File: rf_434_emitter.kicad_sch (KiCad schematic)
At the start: 67 parts, among them J1 Conn_Coaxial, J2 Jack-DC, SW1 SW_DIP_x06, SW5 SW_SPDT, SW7 SW_SPDT, SW8 SW_SPDT, U1 HT12E, U2 TLP-434, U3 LM7805_TO220, X1 ENCODER_ANO

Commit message: DIP switch THT
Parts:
- SW1: footprint Button_Switch_SMD:SW_DIP_SPSTx06_Slide_6.7x16.8mm_W8.61mm_P2.54mm_LowProfile -> Button_Switch_THT:SW_DIP_SPSTx06_Slide_9.78x17.42mm_W7.62mm_P2.54mm
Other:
- moved on the sheet: D1, D10, D11, D12, D2, D3, D4, D5, D6, D7, D8, D9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

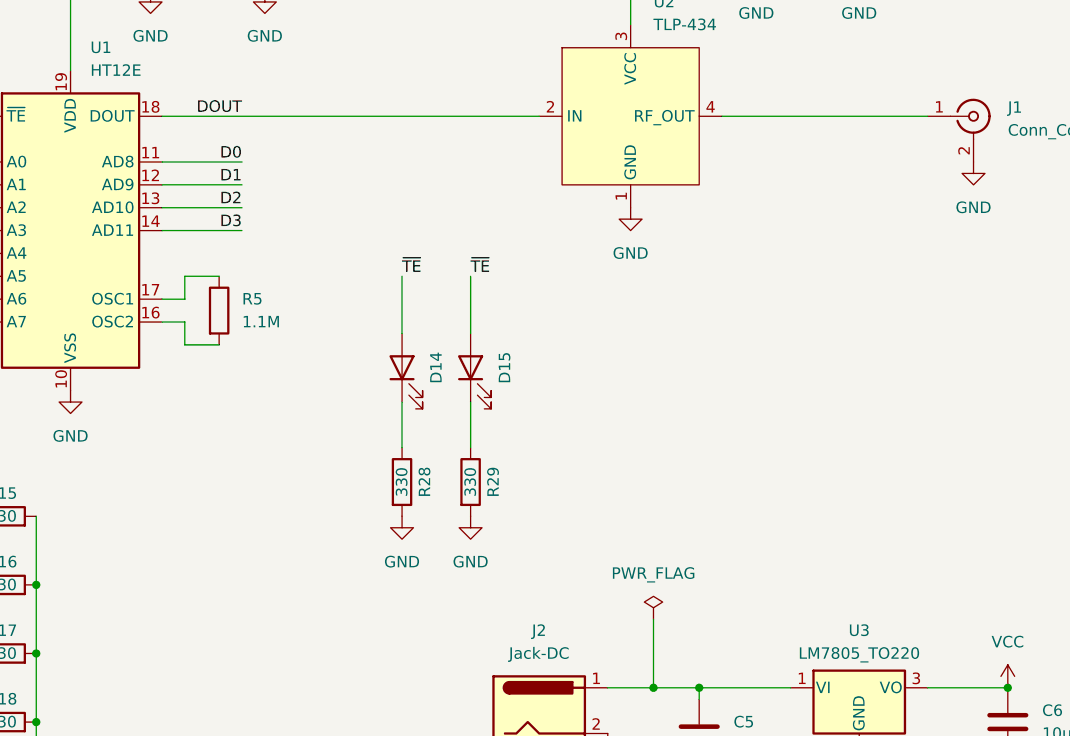
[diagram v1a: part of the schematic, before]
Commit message: Add D0-D3 connector
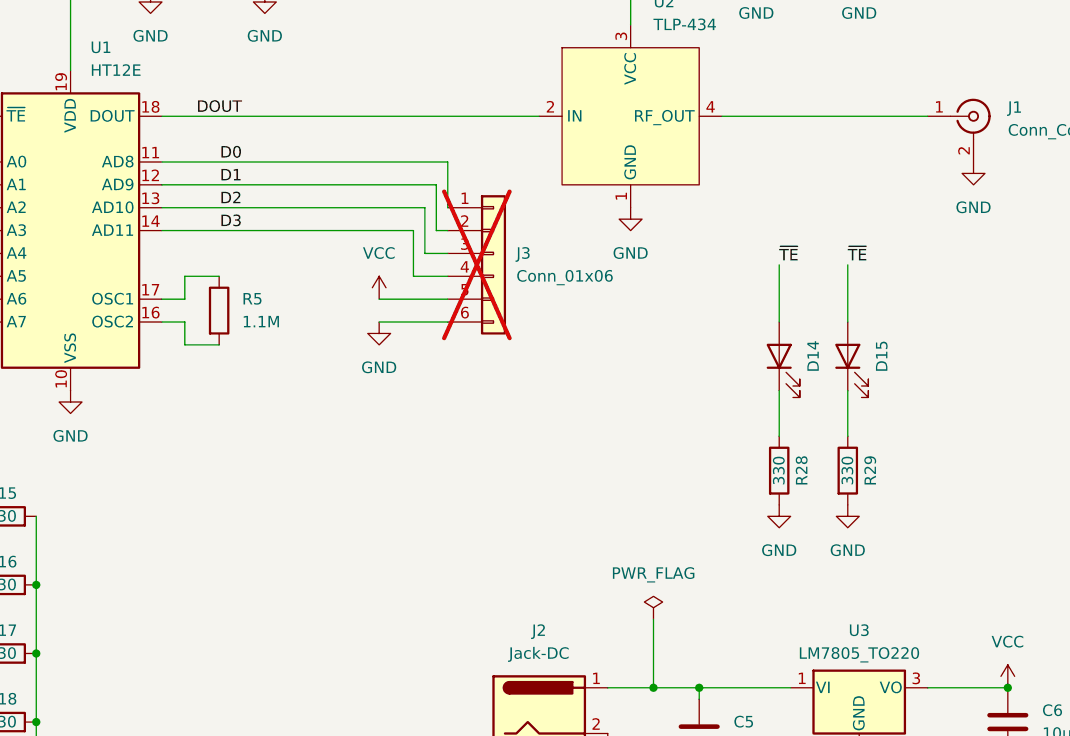
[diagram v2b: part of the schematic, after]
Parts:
- added J3: Conn_01x06, Connector_PinHeader_2.54mm:PinHeader_1x06_P2.54mm_Vertical, symbol Connector_Generic:Conn_01x06
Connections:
- net D0: now also J3.1 (Pin_1)
- net D1: now also J3.2 (Pin_2)
- net D2: now also J3.3 (Pin_3)
- net D3: now also J3.4 (Pin_4)
- net GND: now also J3.6 (Pin_6)
- net VCC: now also J3.5 (Pin_5)
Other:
- moved on the sheet: D14, D15, R28, R29

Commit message: Add 3D model Jack connector
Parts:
- removed J2: Jack-DC, Connector_BarrelJack:BarrelJack_Wuerth_6941xx301002, symbol Connector:Jack-DC
- added J2: Barrel_Jack_Switch, Connector_BarrelJack:BarrelJack_Kycon_KLDX-0202-xC_Horizontal, symbol Connector:Barrel_Jack_Switch
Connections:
- net GND: now also J2.2
- net at C5.1, U3.1 (VI): now also J2.1
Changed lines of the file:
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@@
 		)
 		(instances
-			(project ""
+			(project "rf_434_emitter"
 				(path "/1bcb00bb-9a7f-4a14-b607-a208812fe9e7"
 					(reference "X1")
@@
 		)
 		(instances
-			(project ""
+			(project "rf_434_emitter"
 				(path "/1bcb00bb-9a7f-4a14-b607-a208812fe9e7"
 					(reference "U3")
@@
 		)
 		(instances
-			(project ""
+			(project "rf_434_emitter"
 				(path "/1bcb00bb-9a7f-4a14-b607-a208812fe9e7"
 					(reference "U2")
@@
 		)
 		(instances
-			(project ""
+			(project "rf_434_emitter"
 				(path "/1bcb00bb-9a7f-4a14-b607-a208812fe9e7"
 					(reference "H1")
@@
 		)
 		(instances
-			(project ""
+			(project "rf_434_emitter"
 				(path "/1bcb00bb-9a7f-4a14-b607-a208812fe9e7"
 					(reference "U1")
@@
 		)
 		(instances
-			(project ""
+			(project "rf_434_emitter"
 				(path "/1bcb00bb-9a7f-4a14-b607-a208812fe9e7"
 					(reference "D1")
@@
 		)
 		(instances
-			(project ""
+			(project "rf_434_emitter"
 				(path "/1bcb00bb-9a7f-4a14-b607-a208812fe9e7"
 					(reference "JP1")
@@
 		)
 		(instances
-			(project ""
+			(project "rf_434_emitter"
 				(path "/1bcb00bb-9a7f-4a14-b607-a208812fe9e7"
 					(reference "J1")
@@
 		)
 		(instances
-			(project ""
+			(project "rf_434_emitter"
 				(path "/1bcb00bb-9a7f-4a14-b607-a208812fe9e7"
 					(reference "R9")
@@
 	)
 	(symbol
-		(lib_id "Connector:Jack-DC")
-		(at 194.31 123.19 0)
-		(unit 1)
-		(exclude_from_sim no)
-		(in_bom yes)
-		(on_board yes)
-		(dnp no)
-		(fields_autoplaced yes)
-		(property "Reference" "J2"
-			(at 194.31 114.3 0)
-			(effects
-				(font
-					(size 1.27 1.27)
-				)
-			)
-		)
-		(property "Value" "Jack-DC"
-			(at 194.31 116.84 0)
-			(effects
-				(font
-					(size 1.27 1.27)
-				)
-			)
-		)
-		(property "Footprint" "Connector_BarrelJack:BarrelJack_Wuerth_6941xx301002"
-			(at 195.58 124.206 0)
-			(effects
-				(font
-					(size 1.27 1.27)
-				)
-				(hide yes)
-			)
-		)
-		(property "Datasheet" "~"
-			(at 195.58 124.206 0)
-			(effects
-				(font
-					(size 1.27 1.27)
-				)
-				(hide yes)
-			)
-		)
-		(property "Description" "DC Barrel Jack"
-			(at 194.31 123.19 0)
-			(effects
-				(font
-					(size 1.27 1.27)
-				)
-				(hide yes)
-			)
-		)
-		(pin "2"
-		)
-		(pin "1"
-		)
-		(instances
-			(project ""
-				(path "/1bcb00bb-9a7f-4a14-b607-a208812fe9e7"
-					(reference "J2")
-					(unit 1)
-				)
-			)
-		)
-	)
-	(symbol
 		(lib_id "Connector_Generic:Conn_01x06")
 		(at 189.23 72.39 0)
@@
 		)
 		(instances
-			(project ""
+			(project "rf_434_emitter"
 				(path "/1bcb00bb-9a7f-4a14-b607-a208812fe9e7"
 					(reference "J3")
@@
 	)
 	(symbol
+		(lib_id "Connector:Barrel_Jack_Switch")
+		(at 194.31 123.19 0)
+		(unit 1)
+		(exclude_from_sim no)
+		(in_bom yes)
+		(on_board yes)
+		(dnp no)
+		(fields_autoplaced yes)
+		(property "Reference" "J2"
+			(at 194.31 114.3 0)
+			(effects
+				(font
+					(size 1.27 1.27)
+				)
+			)
+		)
+		(property "Value" "Barrel_Jack_Switch"
+			(at 194.31 116.84 0)
+			(effects
+				(font
+					(size 1.27 1.27)
+				)
+			)
+		)
+		(property "Footprint" "Connector_BarrelJack:BarrelJack_Kycon_KLDX-0202-xC_Horizontal"
+			(at 195.58 124.206 0)
+			(effects
+				(font
+					(size 1.27 1.27)
+				)
+				(hide yes)
+			)
+		)
+		(property "Datasheet" "~"
+			(at 195.58 124.206 0)
+			(effects
+				(font
+					(size 1.27 1.27)
+				)
+				(hide yes)
+			)
+		)
+		(property "Description" "DC Barrel Jack with an internal switch"
+			(at 194.31 123.19 0)
+			(effects
+				(font
+					(size 1.27 1.27)
+				)
+				(hide yes)
+			)
+		)
+		(pin "2"
+		)
+		(pin "3"
+		)
+		(pin "1"
+		)
+		(instances
+			(project "rf_434_emitter"
+				(path "/1bcb00bb-9a7f-4a14-b607-a208812fe9e7"
+					(reference "J2")
+					(unit 1)
+				)
+			)
+		)
+	)
+	(symbol
 		(lib_id "Device:R")
 		(at 220.98 96.52 0)
@@
 		)
 		(instances
-			(project ""
+			(project "rf_434_emitter"
 				(path "/1bcb00bb-9a7f-4a14-b607-a208812fe9e7"
 					(reference "C4")

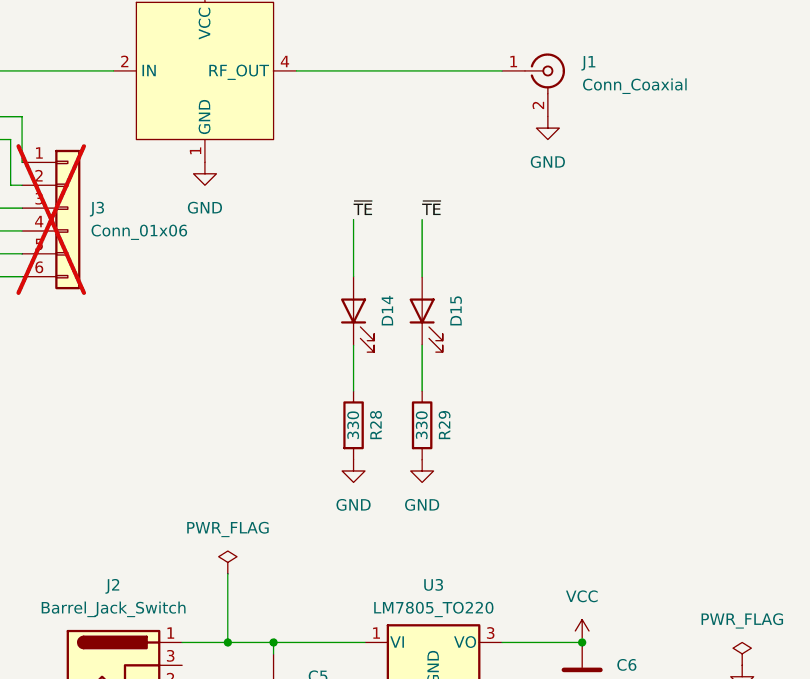
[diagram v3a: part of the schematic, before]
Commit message: Inversion des LED \TE
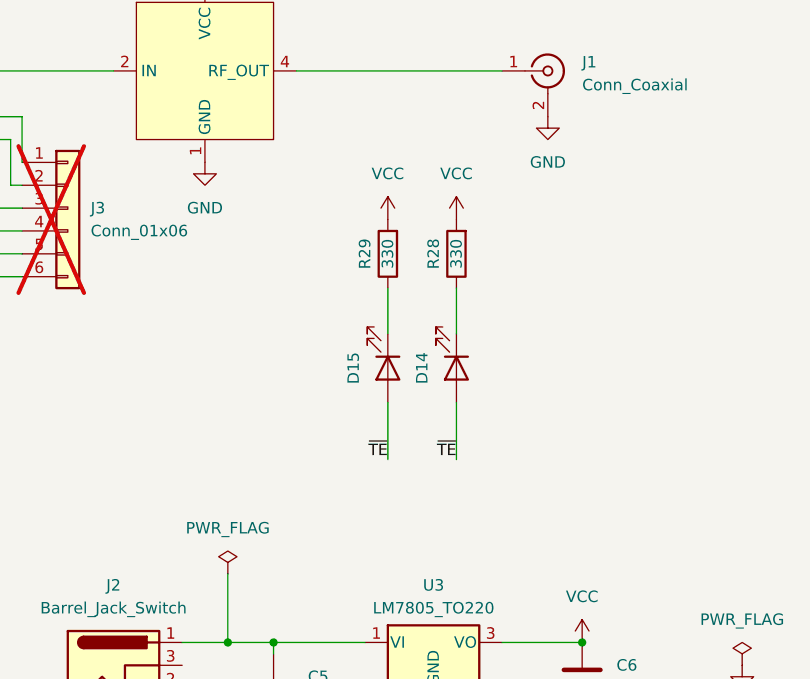
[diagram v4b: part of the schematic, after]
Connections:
- net GND: no longer R28.2, R29.2
- net VCC: now also R28.2, R29.2
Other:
- moved on the sheet: D14, D15, R28, R29

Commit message: ATTENTION
Symbole édité dans le schéma 02 pins à 18 pin
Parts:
- U1: footprint Package_DIP:DIP-20_W7.62mm_Socket -> Package_DIP:DIP-18_W7.62mm_Socket
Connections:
- net A0: now also U1.1 (NC); no longer U1.2 (A0)
- net A1: now also U1.2 (A1); no longer U1.3 (A1)
- net A2: now also U1.3 (A2); no longer U1.4 (A2)
- net A3: now also U1.4 (A3); no longer U1.5 (A3)
- net A4: now also U1.5 (A4); no longer U1.6 (A4)
- net A5: now also U1.6 (A5); no longer U1.7 (A5)
- net A6: now also U1.7 (A6); no longer U1.8 (A6)
- net A7: now also U1.8 (A7); no longer U1.9 (A7)
- net D0: now also U1.10 (AD8); no longer U1.11 (AD8)
- net D1: now also U1.11 (AD9); no longer U1.12 (AD9)
- net D2: now also U1.12 (AD10); no longer U1.13 (AD10)
- net D3: now also U1.13 (AD11); no longer U1.14 (AD11)
- net DOUT: now also U1.17 (DOUT); no longer U1.18 (DOUT)
- net GND: now also U1.9 (VSS); no longer U1.10 (VSS)
- net VCC: now also U1.18 (VDD); no longer U1.19 (VDD)
- net ~{TE}: now also U1.14 (~{TE}); no longer U1.15 (~{TE})
- net at R5.2: now also U1.15 (OSC2); no longer U1.16 (OSC2)
- net at R5.1: now also U1.16 (OSC1); no longer U1.17 (OSC1)
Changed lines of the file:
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@@
 			)
 		)
-		(property "Footprint" "Package_DIP:DIP-20_W7.62mm_Socket"
+		(property "Footprint" "Package_DIP:DIP-18_W7.62mm_Socket"
 			(at 157.48 49.53 0)
 			(effects
@@
 			)
 		)
-		(pin "19"
+		(pin "18"
 		)
 		(pin "3"
@@
 		(pin "15"
 		)
-		(pin "18"
+		(pin "1"
 		)
 		(pin "14"
